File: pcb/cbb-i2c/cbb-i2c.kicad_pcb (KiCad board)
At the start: 2 copper layers, 67.1 x 57.9 mm, 83 parts, among them J1 Conn_02x04_Odd_Even, J14 Screw_Terminal_01x08, J2 Screw_Terminal_01x04, J3 Screw_Terminal_01x06, J4 Screw_Terminal_01x06, J5 Conn_01x04, J6 Conn_01x04, Q1 AO3400A, Q10 AO3400A, Q2 AO3400A, Q3 AO3400A, Q4 AO3400A, Q5 AO3400A, Q6 AO3400A, Q7 AO3400A, Q8 AO3400A, Q9 AO3400A, U1 MCP23017_SS

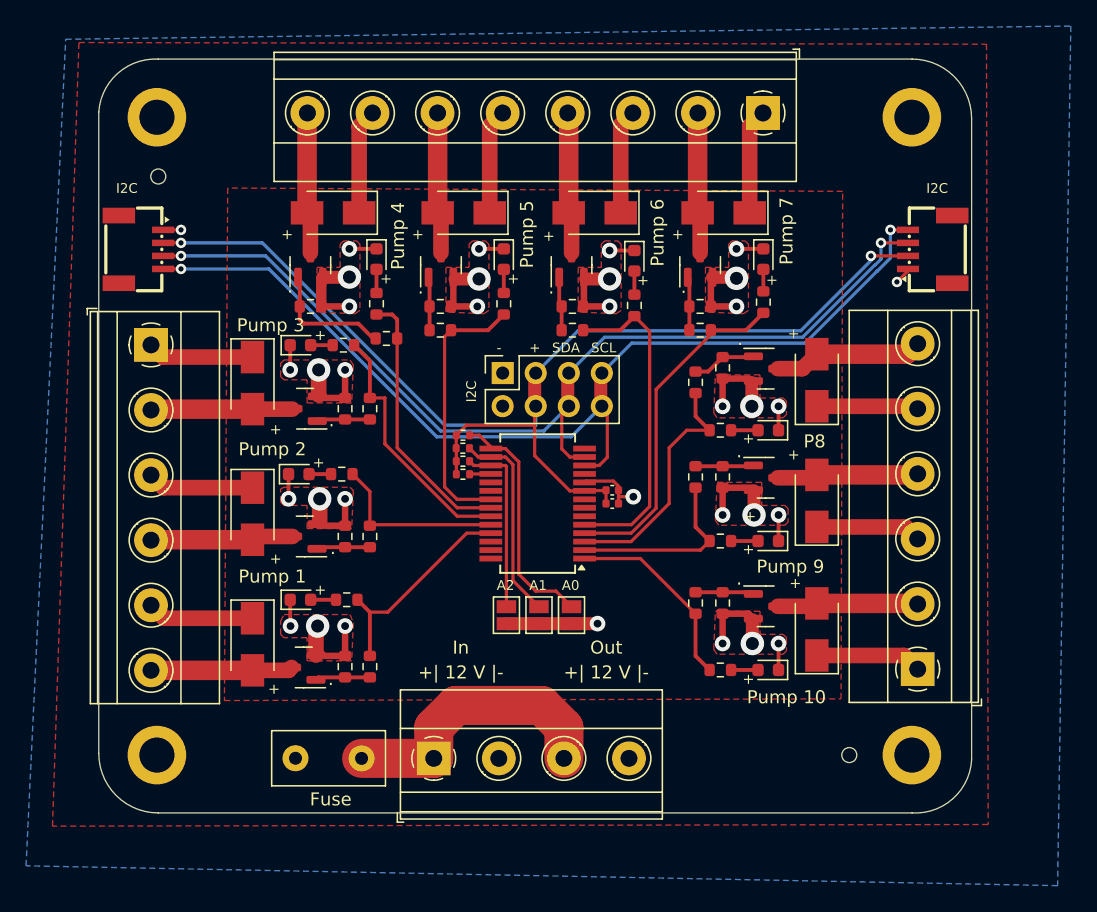
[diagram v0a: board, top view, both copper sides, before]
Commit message: adjust mcp routing
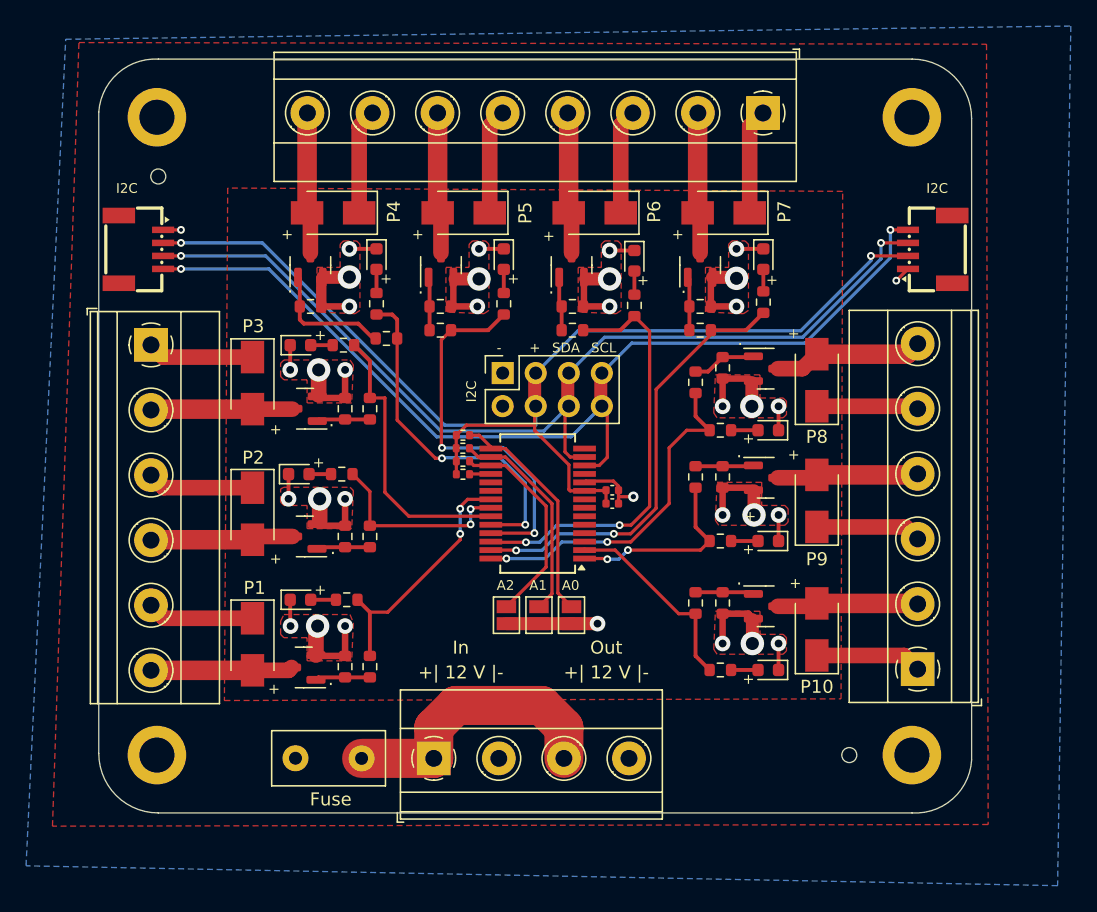
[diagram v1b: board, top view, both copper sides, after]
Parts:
- moved G*** 30.1 mm to (167.0, 73.1)
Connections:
- U1 pad 1: Pump10 -> Pump9
- U1 pad 2: Pump9 -> Pump10
- U1 pad 21: Pump5 -> Pump1
- U1 pad 22: Pump4 -> Pump2
- U1 pad 24: Pump2 -> Pump4
- U1 pad 25: Pump1 -> Pump5
- U1 pad 26: unconnected-(U1-GPA5-Pad26) -> Pump6
- U1 pad 27: unconnected-(U1-GPA6-Pad27) -> Pump7
- U1 pad 28: unconnected-(U1-GPA7-Pad28) -> Pump8
- U1 pad 3: Pump8 -> unconnected-(U1-GPB2-Pad3)
- U1 pad 4: Pump7 -> unconnected-(U1-GPB3-Pad4)
- U1 pad 5: Pump6 -> unconnected-(U1-GPB4-Pad5)
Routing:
- net Pump5: track 20.8 -> 29.6 mm, vias 0 -> 2
- net Pump7: track 25.9 -> 33.9 mm, vias 0 -> 2
- net Pump6: track 25.1 -> 32.9 mm, vias 0 -> 2
- net Pump8: track 19.0 -> 26.7 mm, vias 0 -> 2
- net Pump4: track 20.7 -> 27.2 mm, vias 0 -> 2
- net Pump1: track 16.5 -> 19.1 mm, vias 0 -> 2
- net Net-(JP1-B): track 13.8 -> 16.3 mm
- net Pump3: track 19.7 -> 21.9 mm
- net Pump2: track 13.8 -> 15.2 mm, vias 0 -> 2
- net Net-(JP3-B): track 18.4 -> 17.5 mm
- net Net-(JP2-B): track 15.6 -> 16.4 mm
- net Pump9: track 14.4 -> 14.8 mm, vias 0 -> 2
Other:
- board text added: "P1"
- board text added: "P10"
- board text added: "P2"
- board text added: "P3"
- board text added: "P4"
- board text added: "P5"
- board text added: "P6"
- board text added: "P7"
- board text added: "P9"
- board text removed: "Pump 1"
- board text removed: "Pump 10"
- board text removed: "Pump 2"
- board text removed: "Pump 3"
- board text removed: "Pump 4"
- board text removed: "Pump 5"
- board text removed: "Pump 6"
- board text removed: "Pump 7"
- board text removed: "Pump 9"

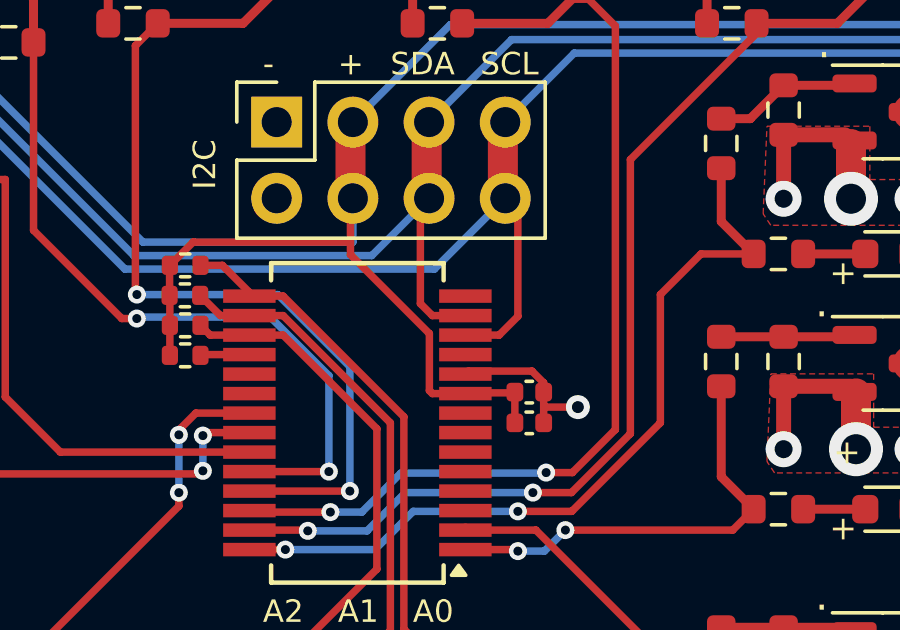
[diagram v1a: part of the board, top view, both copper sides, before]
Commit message: adjust cbb-i2c
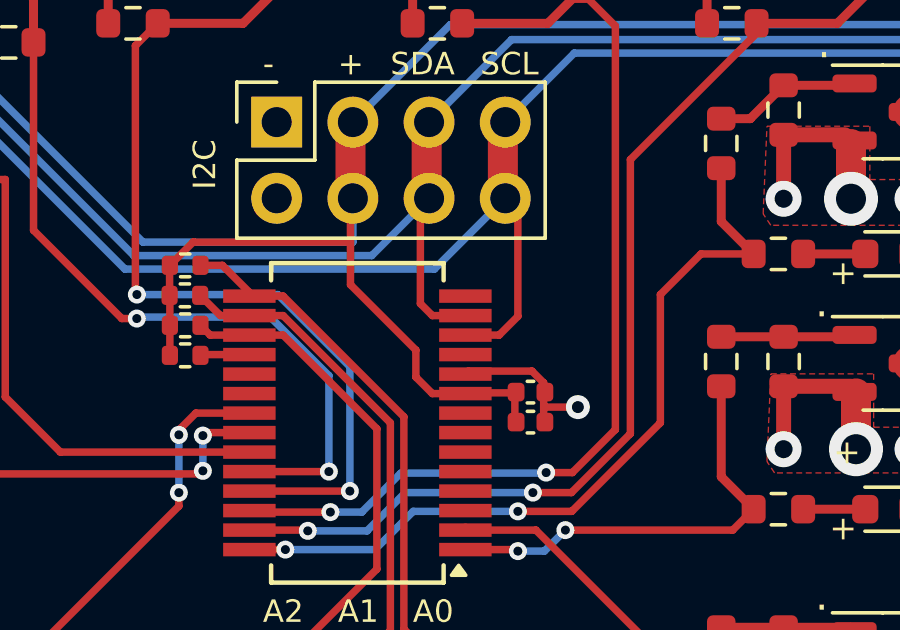
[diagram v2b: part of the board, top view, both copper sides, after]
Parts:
- moved C1 1.03 mm to (193.9, 89.0)
- moved C2 1.00 mm to (193.9, 90.0)
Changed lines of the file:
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@@
 	(footprint "Capacitor_SMD:C_0402_1005Metric"
 		(layer "F.Cu")
-		(at 193.88 89 180)
+		(at 193.92 90 180)
 		(descr "Capacitor SMD 0402 (1005 Metric), square (rectangular) end terminal, IPC_7351 nominal, (Body size source: IPC-SM-782 page 76, https://www.pcb-3d.com/wordpress/wp-content/uploads/ipc-sm-782a_amendment_1_and_2.pdf), generated with kicad-footprint-generator")
 		(tags "capacitor")
@@
 	(footprint "Capacitor_SMD:C_0402_1005Metric"
 		(layer "F.Cu")
-		(at 193.88 90.025 180)
+		(at 193.92 89 180)
 		(descr "Capacitor SMD 0402 (1005 Metric), square (rectangular) end terminal, IPC_7351 nominal, (Body size source: IPC-SM-782 page 76, https://www.pcb-3d.com/wordpress/wp-content/uploads/ipc-sm-782a_amendment_1_and_2.pdf), generated with kicad-footprint-generator")
 		(tags "capacitor")
@@
 	)
 	(segment
+		(start 190.1 87.6)
+		(end 187.92 85.42)
+		(width 0.25)
+		(layer "F.Cu")
+		(net 44)
+	)
+	(segment
 		(start 181.9 87.775)
 		(end 181.9 86.775)
@@
 	)
 	(segment
-		(start 190.65 89.05)
-		(end 190.55 88.95)
-		(width 0.25)
-		(layer "F.Cu")
-		(net 44)
-	)
-	(segment
 		(start 191.775 89.025)
 		(end 191.75 89.05)
@@
 	)
 	(segment
-		(start 190.55 88.95)
-		(end 190.55 87.05)
+		(start 182.675 84)
+		(end 187.92 84)
 		(width 0.25)
 		(layer "F.Cu")
@@
 	)
 	(segment
-		(start 182.675 84)
-		(end 187.92 84)
+		(start 190.65 89.05)
+		(end 190.1 88.5)
 		(width 0.25)
 		(layer "F.Cu")
@@
 	)
 	(segment
-		(start 190.55 87.05)
-		(end 187.92 84.42)
+		(start 187.92 85.42)
+		(end 187.92 82.54)
 		(width 0.25)
 		(layer "F.Cu")
@@
 	)
 	(segment
-		(start 187.92 84.42)
-		(end 187.92 82.54)
+		(start 216.975 71)
+		(end 213.75 71)
 		(width 0.25)
 		(layer "F.Cu")
@@
 	)
 	(segment
-		(start 216.975 71)
-		(end 213.75 71)
+		(start 190.1 88.5)
+		(end 190.1 87.6)
 		(width 0.25)
 		(layer "F.Cu")

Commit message: add power indicator led to cbb i2c
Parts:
- added D21: LED, LED_SMD:LED_0603_1608Metric, F.Cu at (181.7, 80.3)
- added R22: 220, Resistor_SMD:R_0603_1608Metric, F.Cu at (181.7, 82.0)
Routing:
- net GND: track 97.1 -> 100.2 mm
- net +3V3: track 93.1 -> 95.2 mm
- net Net-(D21-A): track 0.00 -> 1.72 mm
- net Pump5: track 29.6 -> 30.9 mm
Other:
- board text added: "CocktailBerryBoard I2C v0.2 08/2026"
- board text removed: "CocktailBerryBoard I2C v0.1 07/2026"

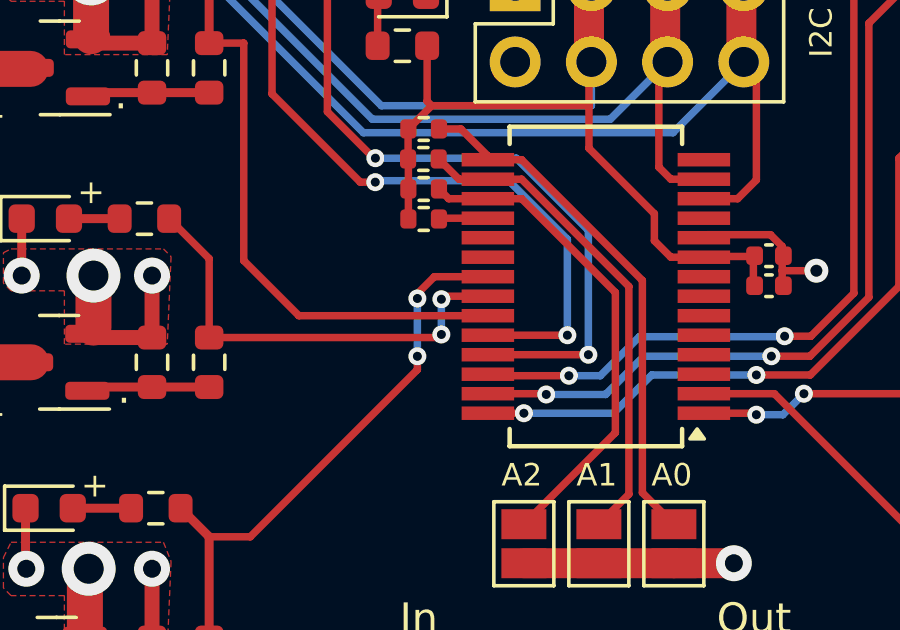
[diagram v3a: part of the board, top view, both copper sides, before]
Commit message: reduce brightness of channel indicator led
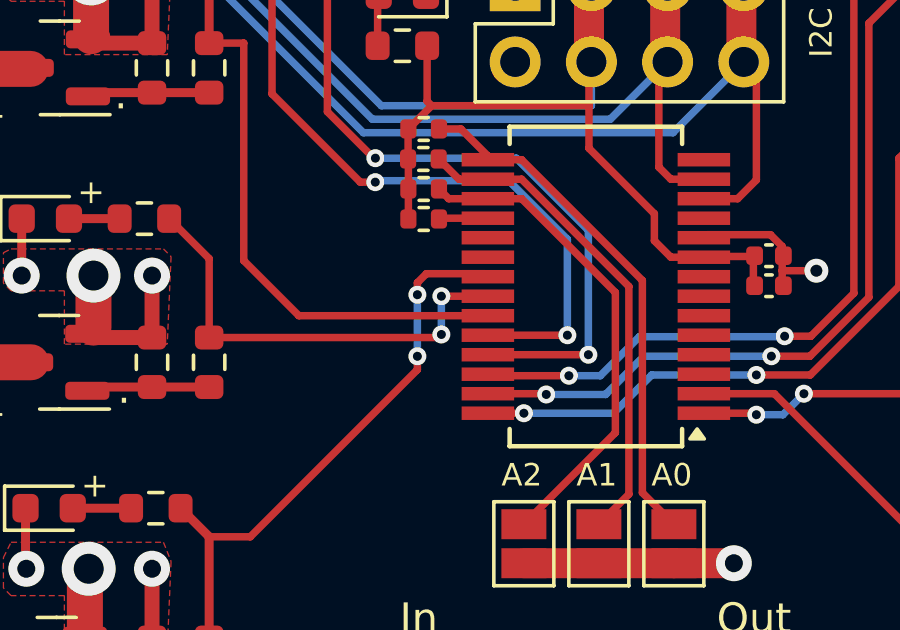
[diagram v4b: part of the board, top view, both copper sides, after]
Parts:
- R12, R13, R14, R15, R16, R17, R18, R19, R20, R21: value 220 -> 680
- R22: value 220 -> 820
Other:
- board text added: "CocktailBerryBoard I2C v1.0 09/2026"
- board text removed: "CocktailBerryBoard I2C v0.2 08/2026"
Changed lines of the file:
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@@
 			)
 		)
-		(property "Value" "220"
+		(property "Value" "680"
 			(at 0 1.43 90)
 			(layer "F.Fab")
@@
 			)
 		)
-		(property "MPN" "C22962"
+		(property "MPN" "C23228"
 			(at 0 0 90)
 			(unlocked yes)
@@
 			)
 		)
-		(property "Value" "220"
+		(property "Value" "680"
 			(at 0 1.43 90)
 			(layer "F.Fab")
@@
 			)
 		)
-		(property "MPN" "C22962"
+		(property "MPN" "C23228"
 			(at 0 0 90)
 			(unlocked yes)
@@
 			)
 		)
-		(property "Value" "220"
+		(property "Value" "680"
 			(at 0 1.43 0)
 			(layer "F.Fab")
@@
 			)
 		)
-		(property "MPN" "C22962"
+		(property "MPN" "C23228"
 			(at 0 0 180)
 			(unlocked yes)
@@
 			)
 		)
-		(property "Value" "220"
+		(property "Value" "820"
 			(at 0 1.43 0)
 			(layer "F.Fab")
@@
 			)
 		)
-		(property "MPN" "C22962"
+		(property "MPN" "C23253"
 			(at 0 0 0)
 			(unlocked yes)
@@
 			)
 		)
-		(property "Value" "220"
+		(property "Value" "680"
 			(at 0 1.43 0)
 			(layer "F.Fab")
@@
 			)
 		)
-		(property "MPN" "C22962"
+		(property "MPN" "C23228"
 			(at 0 0 180)
 			(unlocked yes)
@@
 			)
 		)
-		(property "Value" "220"
+		(property "Value" "680"
 			(at 0 1.43 90)
 			(layer "F.Fab")
@@
 			)
 		)
-		(property "MPN" "C22962"
+		(property "MPN" "C23228"
 			(at 0 0 90)
 			(unlocked yes)
@@
 			)
 		)
-		(property "Value" "220"
+		(property "Value" "680"
 			(at 0 1.43 0)
 			(layer "F.Fab")
@@
 			)
 		)
-		(property "MPN" "C22962"
+		(property "MPN" "C23228"
 			(at 0 0 0)
 			(unlocked yes)
@@
 			)
 		)
-		(property "Value" "220"
+		(property "Value" "680"
 			(at 0 1.43 90)
 			(layer "F.Fab")
@@
 			)
 		)
-		(property "MPN" "C22962"
+		(property "MPN" "C23228"
 			(at 0 0 90)
 			(unlocked yes)
@@
 			)
 		)
-		(property "Value" "220"
+		(property "Value" "680"
 			(at 0 1.43 0)
 			(layer "F.Fab")
@@
 			)
 		)
-		(property "MPN" "C22962"
+		(property "MPN" "C23228"
 			(at 0 0 0)
 			(unlocked yes)
@@
 		(tags "LED")
 		(property "Reference" "D21"
-			(at 0 -1.43 360)
+			(at 0 -1.43 0)
 			(layer "F.SilkS")
 			(hide yes)
@@
 		)
 		(property "Value" "LED"
-			(at 0 1.43 360)
+			(at 0 1.43 0)
 			(layer "F.Fab")
 			(effects
@@
 		)
 		(fp_text user "${REFERENCE}"
-			(at 0 0 360)
+			(at 0 0 0)
 			(layer "F.Fab")
 			(effects
@@
 			)
 		)
-		(property "Value" "220"
+		(property "Value" "680"
 			(at 0 1.43 0)
 			(layer "F.Fab")
@@
 			)
 		)
-		(property "MPN" "C22962"
+		(property "MPN" "C23228"
 			(at 0 0 0)
 			(unlocked yes)
@@
 			)
 		)
-		(property "Value" "220"
+		(property "Value" "680"
 			(at 0 1.43 0)
 			(layer "F.Fab")
@@
 			)
 		)
-		(property "MPN" "C22962"
+		(property "MPN" "C23228"
 			(at 0 0 180)
 			(unlocked yes)
@@
 		)
 	)
-	(gr_text "CocktailBerryBoard\nI2C v0.2\n08/2026"
+	(gr_text "CocktailBerryBoard\nI2C v1.0\n09/2026"
 		(at 187.75 64.75 0)
 		(layer "B.SilkS")
@@
 	)
 	(via
-		(at 183 90.45)
+		(at 183 90.35)
 		(size 0.6)
 		(drill 0.3)
@@
 	)
 	(segment
-		(start 182.2 90.375)
-		(end 182.2 90.266116)
-		(width 0.25)
-		(layer "F.Cu")
-		(net 42)
-	)
-	(segment
-		(start 182.2 90.266116)
-		(end 182.766116 89.7)
+		(start 176.631209 98.368791)
+		(end 175.26 98.368791)
 		(width 0.25)
 		(layer "F.Cu")
@@
 	)
 	(segment
-		(start 182.766116 89.7)
-		(end 184.55 89.7)
+		(start 182.2 89.9)
+		(end 182.5 89.6)
 		(width 0.25)
 		(layer "F.Cu")
@@
 	)
 	(segment
-		(start 176.631209 98.368791)
-		(end 175.26 98.368791)
+		(start 182.5 89.6)
+		(end 184.45 89.6)
 		(width 0.25)
 		(layer "F.Cu")
@@
 	)
 	(segment
+		(start 182.2 90.3)
+		(end 182.2 89.9)
+		(width 0.25)
+		(layer "F.Cu")
+		(net 42)
+	)
+	(segment
+		(start 184.45 89.6)
+		(end 184.55 89.7)
+		(width 0.25)
+		(layer "F.Cu")
+		(net 42)
+	)
+	(segment
 		(start 182.2 92.8)
 		(end 176.631209 98.368791)
@@
 	)
 	(via
-		(at 182.2 90.425)
+		(at 182.2 90.3)
 		(size 0.6)
 		(drill 0.3)
@@
 	(segment
 		(start 182.2 92.352)
-		(end 182.2 90.375)
+		(end 182.2 90.3)
 		(width 0.25)
 		(layer "B.Cu")
